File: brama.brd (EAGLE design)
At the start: 101.6 x 100 mm, 50 parts, among them IC1 AT90USB162A, J1 AVR_SPI_PRG_6OFFSET_PADS

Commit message: większe miejsce na fona
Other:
- board size 101.6 x 100 mm -> 104.1 x 126.7 mm
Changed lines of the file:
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@@
 <?xml version="1.0" encoding="utf-8"?>
 <!DOCTYPE eagle SYSTEM "eagle.dtd">
-<eagle version="6.3">
+<eagle version="6.4">
 <drawing>
 <settings>
@@
 <setting verticaltext="up"/>
 </settings>
-<grid distance="0.05" unitdist="inch" unit="inch" style="lines" multiple="1" display="no" altdistance="0.005" altunitdist="inch" altunit="inch"/>
+<grid distance="0.05" unitdist="inch" unit="mm" style="lines" multiple="1" display="no" altdistance="0.005" altunitdist="inch" altunit="mm"/>
 <layers>
 <layer number="1" name="Top" color="4" fill="1" visible="yes" active="yes"/>
@@
 <board>
 <plain>
-<wire x1="0" y1="0" x2="101.58" y2="1.27" width="0" layer="20"/>
-<wire x1="101.58" y1="1.27" x2="101.58" y2="100" width="0" layer="20"/>
-<wire x1="101.58" y1="100" x2="0" y2="100" width="0" layer="20"/>
-<wire x1="0" y1="100" x2="0" y2="0" width="0" layer="20"/>
-<wire x1="58.42" y1="77.47" x2="90.17" y2="77.47" width="0.4064" layer="20"/>
-<wire x1="90.17" y1="77.47" x2="90.17" y2="12.7" width="0.4064" layer="20"/>
-<wire x1="90.17" y1="12.7" x2="58.42" y2="12.7" width="0.4064" layer="20"/>
-<wire x1="58.42" y1="12.7" x2="58.42" y2="77.47" width="0.4064" layer="20"/>
+<wire x1="-1.27" y1="-25.4" x2="102.85" y2="-25.4" width="0" layer="20"/>
+<wire x1="102.85" y1="-25.4" x2="102.85" y2="100" width="0" layer="20"/>
+<wire x1="102.85" y1="100" x2="-1.27" y2="101.27" width="0" layer="20"/>
+<wire x1="-1.27" y1="101.27" x2="-1.27" y2="-25.4" width="0" layer="20"/>
+<wire x1="58.42" y1="77.47" x2="99.06" y2="77.47" width="0.4064" layer="20"/>
+<wire x1="99.06" y1="77.47" x2="99.06" y2="-22.86" width="0.4064" layer="20"/>
+<wire x1="99.06" y1="-22.86" x2="58.42" y2="-22.86" width="0.4064" layer="20"/>
+<wire x1="58.42" y1="-22.86" x2="58.42" y2="77.47" width="0.4064" layer="20"/>
+<dimension x1="58.42" y1="77.47" x2="99.06" y2="77.47" x3="78.74" y3="77.47" textsize="1.778" layer="16"/>
+<dimension x1="58.42" y1="77.47" x2="58.42" y2="-22.86" x3="58.42" y3="27.305" textsize="1.778" layer="16"/>
 </plain>
 <attributes>
@@
 <polygon width="0.254" layer="16" isolate="0.3048">
 <vertex x="8.89" y="90.17"/>
-<vertex x="92.71" y="90.17"/>
-<vertex x="92.71" y="10.16"/>
-<vertex x="8.89" y="10.16"/>
+<vertex x="101.6" y="90.17"/>
+<vertex x="101.6" y="-24.13"/>
+<vertex x="8.89" y="-24.13"/>
 </polygon>
 <wire x1="76.835" y1="81.28" x2="77.155" y2="81.6" width="0.4064" layer="16"/>
@@
 <contactref element="JP4" pad="1"/>
 <contactref element="JP5" pad="1"/>
+<wire x1="43.881" y1="81.28" x2="43.434" y2="76.454" width="0" layer="19" extent="16-16"/>
 </signal>
 <signal name="5V">

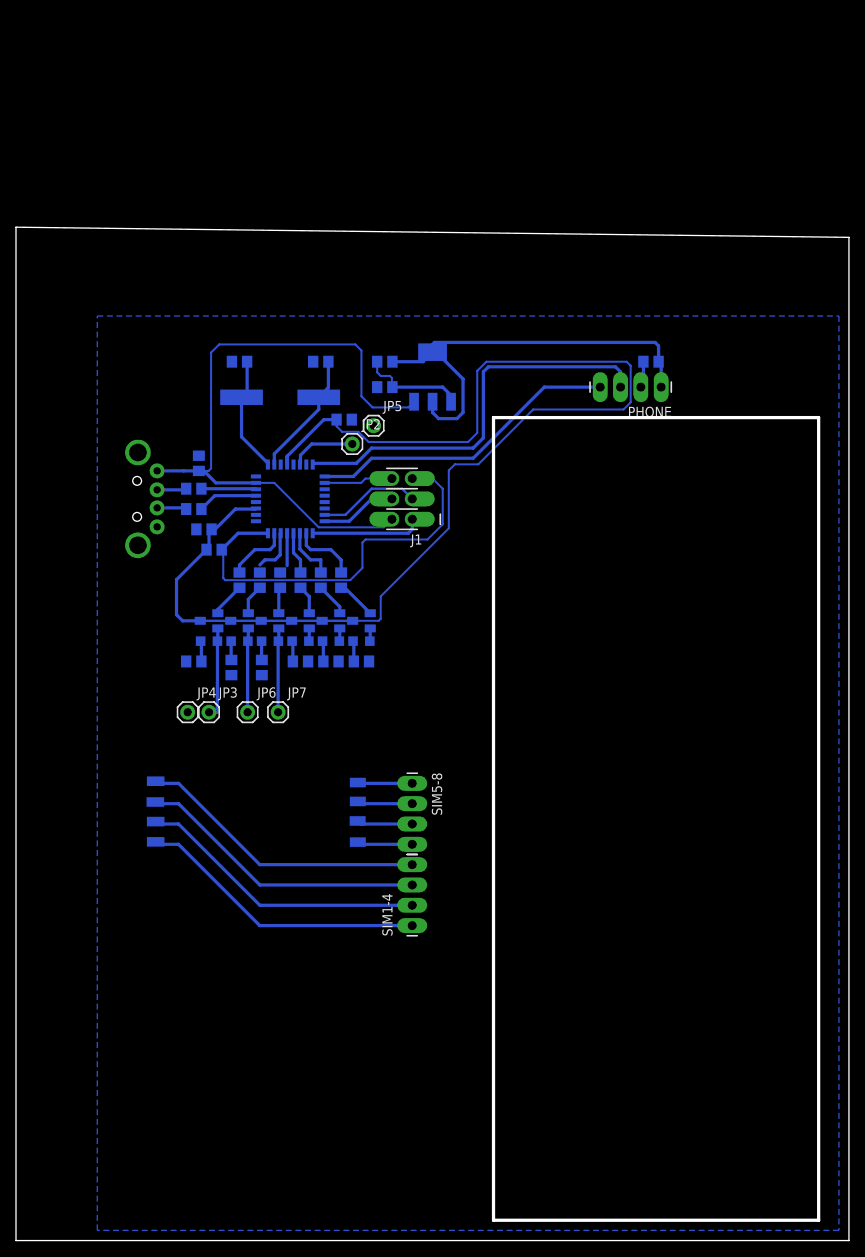
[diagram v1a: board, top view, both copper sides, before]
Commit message: Mounting Holes + Autor Sign + AT Command Set PDF
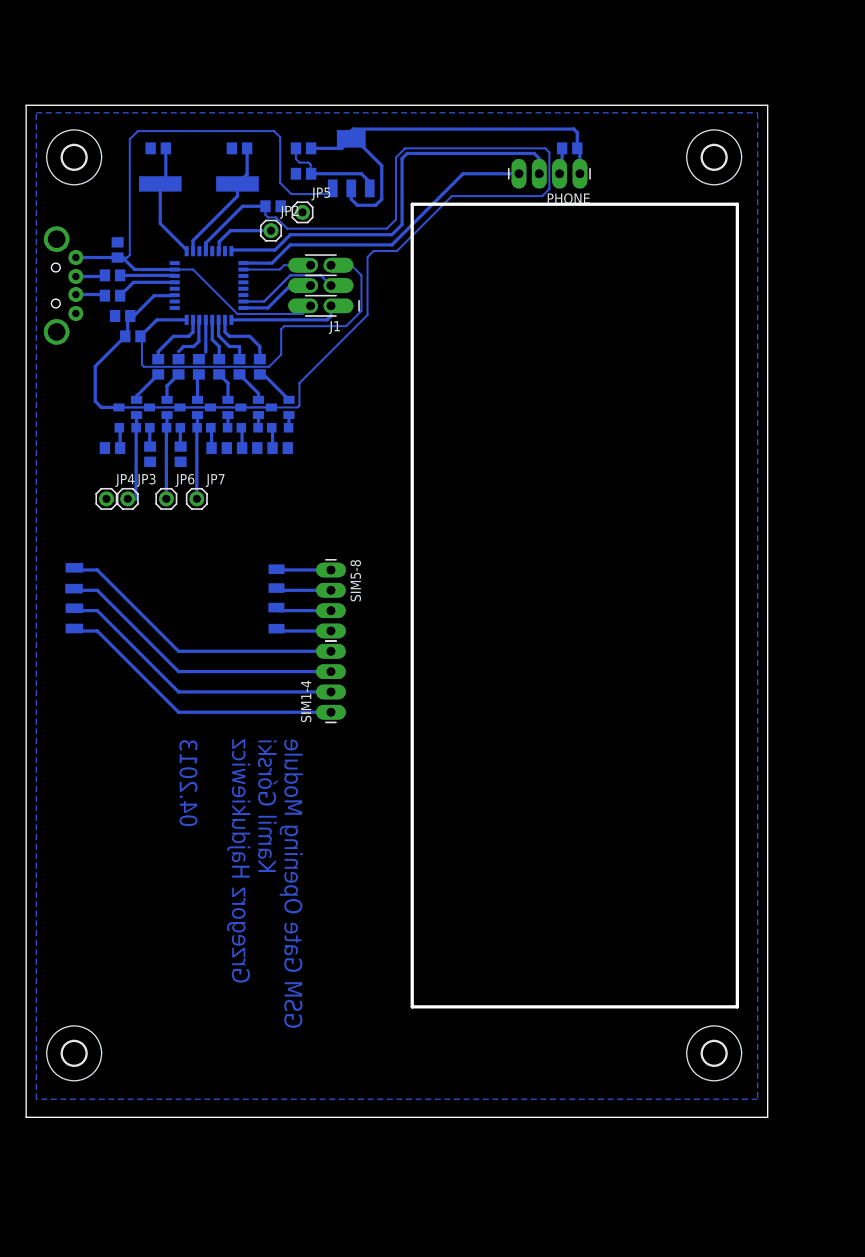
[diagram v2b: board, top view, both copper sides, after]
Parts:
- added U$2, U$3, U$4, U$5: (no value), holes:3,0
- moved C1 28.5 mm to (12.1, 90.2)
- moved C6 28.5 mm to (67.9, 111.1)
- moved IC1 28.5 mm to (22.9, 94.0)
- moved J1 28.5 mm to (36.8, 94.0)
- moved JP4 28.5 mm to (10.0, 67.3)
- moved R16 28.5 mm to (34.7, 111.1)
- moved R17 28.5 mm to (34.7, 108.0)
- moved C2 28.5 mm to (16.5, 111.1)
- moved C3 28.5 mm to (26.7, 111.1)
- moved C4 28.5 mm to (11.4, 98.4)
- moved IC2 28.5 mm to (40.6, 109.2)
- moved JP1 28.5 mm to (3.81, 94.0)
- moved JP3 28.5 mm to (12.7, 67.3)
- moved JP6 28.5 mm to (17.5, 67.3)
- moved JP7 28.5 mm to (21.3, 67.3)
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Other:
- board size 104.1 x 126.7 mm -> 92.7 x 126.5 mm
- board text added: "GSM Gate Opening Module Kamil Górski Grzegorz Hajdukiewicz 04.2013"

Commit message: DC-DC converter
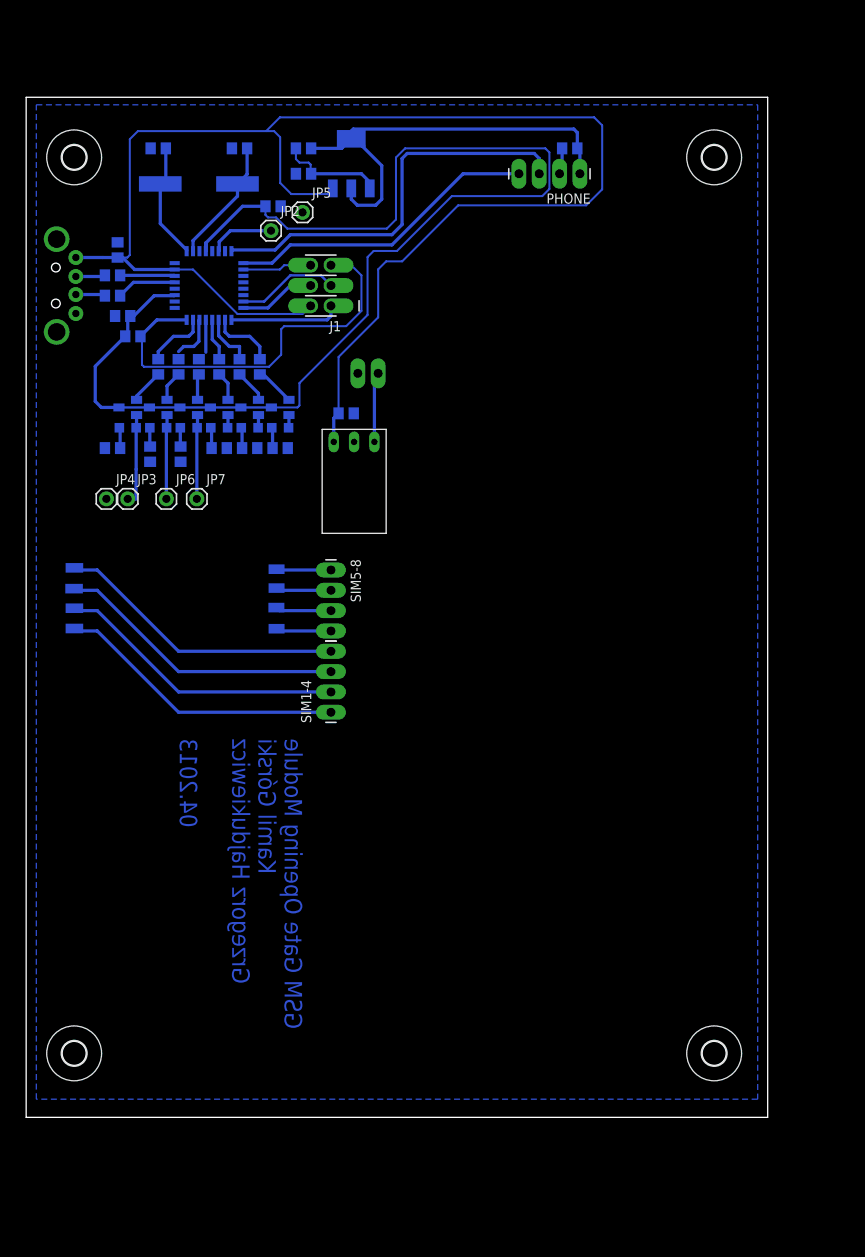
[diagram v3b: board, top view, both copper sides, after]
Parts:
- added C7: 33n, rcl:C0805
- added JP8: (no value), SparkFun-Connectors:1X02_LONGPADS
- added U$6: U3V12F12, pololu DC-DC converters:THT
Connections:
- new net 12V: JP8.1, U$6.VOUT
- net 5V: now also C7.2, U$6.VIN
- net GND: now also C7.1, JP8.2, U$6.GND
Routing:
- net 5V: track 81.5 -> 188.7 mm
- net 12V: track 0.00 -> 8.76 mm
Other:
- board size 92.7 x 126.5 mm -> 92.7 x 127.5 mm
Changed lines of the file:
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@@
 <setting verticaltext="up"/>
 </settings>
-<grid distance="10" unitdist="mm" unit="mm" style="lines" multiple="1" display="yes" altdistance="1" altunitdist="mm" altunit="mm"/>
+<grid distance="1.27" unitdist="mm" unit="inch" style="lines" multiple="1" display="yes" altdistance="0.003937" altunitdist="inch" altunit="inch"/>
 <layers>
 <layer number="1" name="Top" color="4" fill="1" visible="yes" active="yes"/>
@@
 <plain>
 <wire x1="0" y1="-10" x2="92.69" y2="-10" width="0" layer="20"/>
-<wire x1="92.69" y1="-10" x2="92.69" y2="116.51" width="0" layer="20"/>
-<wire x1="92.69" y1="116.51" x2="0" y2="116.51" width="0" layer="20"/>
-<wire x1="0" y1="116.51" x2="0" y2="-10" width="0" layer="20"/>
-<wire x1="48.26" y1="104.14" x2="88.9" y2="104.14" width="0.4064" layer="20"/>
-<wire x1="88.9" y1="104.14" x2="88.9" y2="3.81" width="0.4064" layer="20"/>
-<wire x1="88.9" y1="3.81" x2="48.26" y2="3.81" width="0.4064" layer="20"/>
-<wire x1="48.26" y1="3.81" x2="48.26" y2="104.14" width="0.4064" layer="20"/>
+<wire x1="92.69" y1="-10" x2="92.69" y2="117.51" width="0" layer="20"/>
+<wire x1="92.69" y1="117.51" x2="0" y2="117.51" width="0" layer="20"/>
+<wire x1="0" y1="117.51" x2="0" y2="-10" width="0" layer="20"/>
 <text x="34.49" y="37.37" size="2.1844" layer="16" rot="MR270">GSM Gate Opening Module
 Kamil Górski
@@
 <element name="U$4" library="holes" package="3,0" value="" x="86" y="110"/>
 <element name="U$5" library="holes" package="3,0" value="" x="6" y="-2"/>
+<element name="U$6" library="pololu DC-DC converters" package="THT" value="U3V12F12" x="45" y="63" rot="R90"/>
+<element name="C7" library="rcl" package="C0805" value="33n" x="40" y="78" rot="MR0"/>
+<element name="JP8" library="SparkFun-Connectors" package="1X02_LONGPADS" value="" x="44" y="83" rot="R180"/>
 </elements>
 <signals>
@@
 <wire x1="31.718" y1="95.98" x2="27.1526" y2="95.98" width="0.254" layer="16"/>
 <polygon width="0.254" layer="16" isolate="0.3048">
-<vertex x="1.27" y="115.57"/>
-<vertex x="91.44" y="115.57"/>
+<vertex x="1.27" y="116.57"/>
+<vertex x="91.44" y="116.57"/>
 <vertex x="91.44" y="-7.73"/>
 <vertex x="1.27" y="-7.73"/>
@@
 <contactref element="JP4" pad="1"/>
 <contactref element="JP5" pad="1"/>
+<contactref element="U$6" pad="GND"/>
+<contactref element="C7" pad="1"/>
+<contactref element="JP8" pad="2"/>
 </signal>
 <signal name="5V">
@@
 <wire x1="33.147" y1="105.41" x2="31.75" y2="106.807" width="0.254" layer="16"/>
 <wire x1="31.75" y1="106.807" x2="31.75" y2="112.522" width="0.254" layer="16"/>
-<wire x1="13.97" y1="113.284" x2="30.988" y2="113.284" width="0.254" layer="16"/>
+<wire x1="13.97" y1="113.284" x2="30" y2="113.284" width="0.254" layer="16"/>
+<wire x1="30" y1="113.284" x2="30.988" y2="113.284" width="0.254" layer="16"/>
 <wire x1="30.988" y1="113.284" x2="31.75" y2="112.522" width="0.254" layer="16"/>
 <wire x1="13.97" y1="113.284" x2="12.954" y2="112.268" width="0.254" layer="16"/>
@@
 <wire x1="12.639" y1="97.475" x2="11.43" y2="97.475" width="0.254" layer="16"/>
 <wire x1="38.3286" y1="106.1212" x2="37.6174" y2="105.41" width="0.254" layer="16"/>
+<contactref element="U$6" pad="VIN"/>
+<contactref element="C7" pad="2"/>
+<wire x1="38.45" y1="74.43" x2="38.45" y2="77.4" width="0.4064" layer="16"/>
+<wire x1="38.45" y1="77.4" x2="39.05" y2="78" width="0.4064" layer="16"/>
+<wire x1="39.05" y1="78" x2="39.05" y2="85.05" width="0.254" layer="16"/>
+<wire x1="39.05" y1="85.05" x2="44" y2="90" width="0.254" layer="16"/>
+<wire x1="44" y1="90" x2="44" y2="96" width="0.254" layer="16"/>
+<wire x1="44" y1="96" x2="45" y2="97" width="0.254" layer="16"/>
+<wire x1="45" y1="97" x2="47" y2="97" width="0.254" layer="16"/>
+<wire x1="47" y1="97" x2="54" y2="104" width="0.254" layer="16"/>
+<wire x1="54" y1="104" x2="70" y2="104" width="0.254" layer="16"/>
+<wire x1="70" y1="104" x2="72" y2="106" width="0.254" layer="16"/>
+<wire x1="72" y1="106" x2="72" y2="114" width="0.254" layer="16"/>
+<wire x1="72" y1="114" x2="71" y2="115" width="0.254" layer="16"/>
+<wire x1="71" y1="115" x2="31.716" y2="115" width="0.254" layer="16"/>
+<wire x1="31.716" y1="115" x2="30" y2="113.284" width="0.254" layer="16"/>
 </signal>
 <signal name="RESET">
@@
 <wire x1="19.05" y1="85.725" x2="19.05" y2="84.77" width="0" layer="19" extent="16-16"/>
 </signal>
+<signal name="12V">
+<contactref element="U$6" pad="VOUT"/>
+<contactref element="JP8" pad="1"/>
+<wire x1="43.53" y1="74.43" x2="43.53" y2="82.53" width="0.4064" layer="16"/>
+<wire x1="43.53" y1="82.53" x2="44" y2="83" width="0.4064" layer="16"/>
+</signal>
 </signals>
